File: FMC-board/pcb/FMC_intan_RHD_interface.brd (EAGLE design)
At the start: 76.5 x 69 mm, 84 parts, among them Q1 SSM3J328R, U1 4901, U2 7933, U3 ADN4663, U4 ADN4663, U5 ADN4664, U6 PDS1, U7 4901, U8 FMC_SINGLE_WIDTH_MODULE

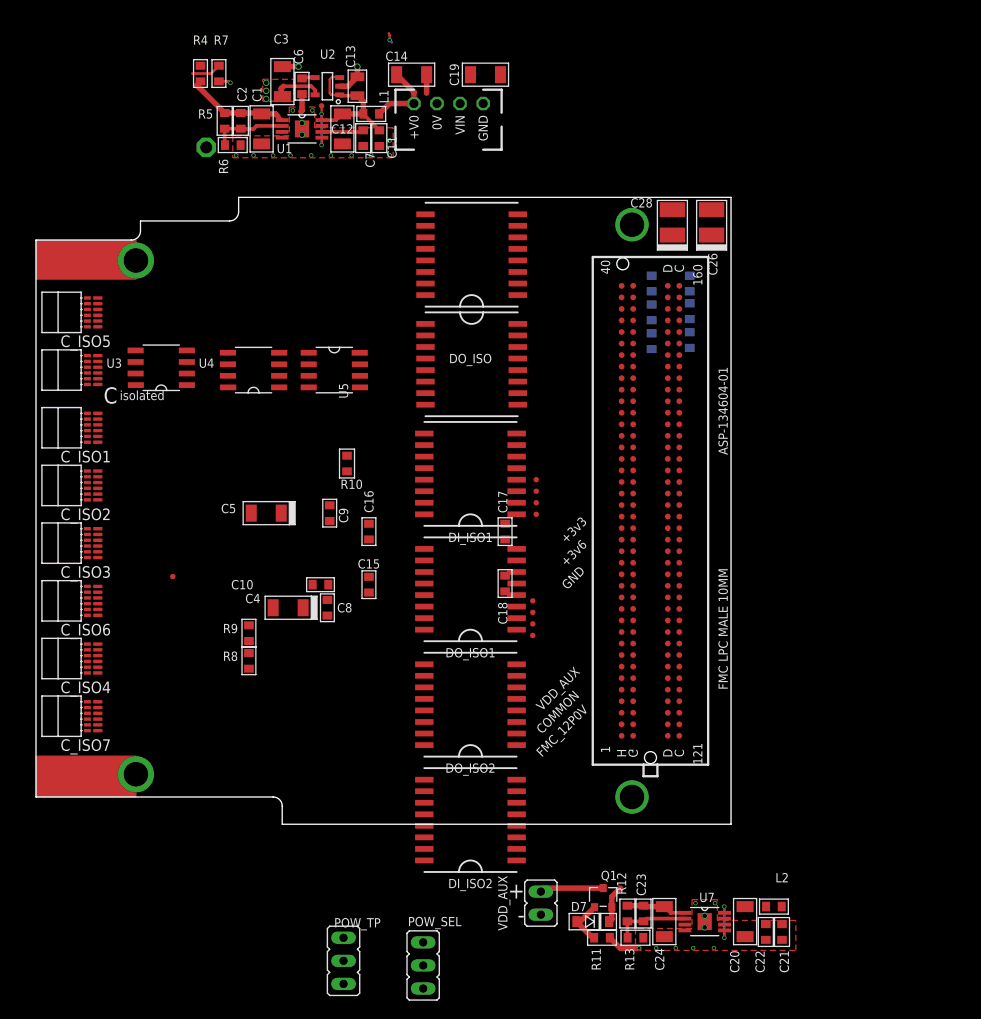
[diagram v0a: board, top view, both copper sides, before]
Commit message: added some cmos/lvds bridge components to check spacing
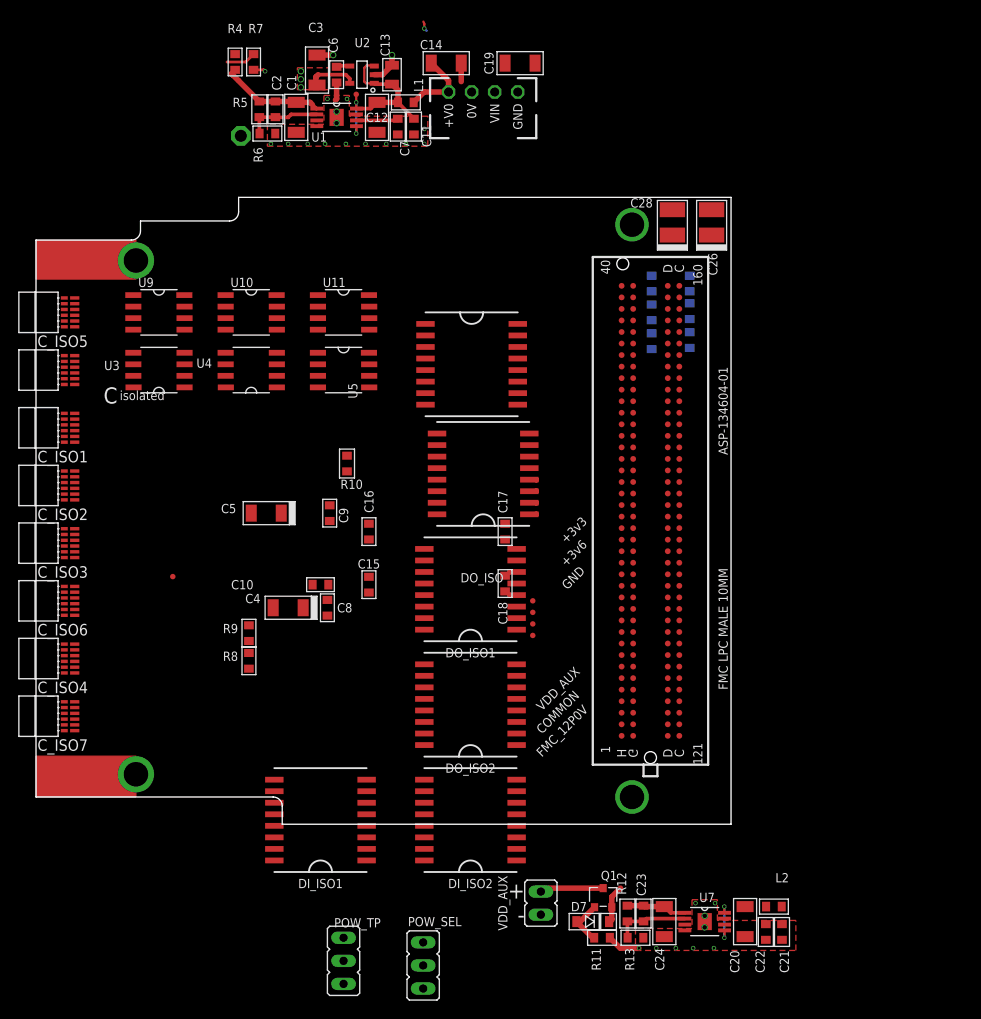
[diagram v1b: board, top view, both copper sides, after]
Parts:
- added U10, U11: ADN4663, jonnew:SOIC127P500X400-8N
- added U9: ADN4664, jonnew:SOIC127P500X400-8N
- moved DI_ISO1 41.5 mm to (-34.3, -2.54)
- moved DO_ISO 24.2 mm to (-16.4, 35.6)
- moved C14 4.02 mm to (-20.4, 80.8)
- moved C3 4.02 mm to (-34.7, 80.0)
- moved C7 4.02 mm to (-25.8, 73.8)
- moved R6 4.02 mm to (-40.1, 73.0)
- moved C19 4.02 mm to (-12.3, 80.8)
- moved C11 4.02 mm to (-24.0, 73.8)
- moved C1 4.02 mm to (-37.0, 74.8)
- moved C6 4.02 mm to (-32.5, 79.5)
- moved L1 4.02 mm to (-24.9, 76.5)
- moved R5 4.02 mm to (-41.0, 75.7)
- moved R7 4.02 mm to (-41.7, 80.9)
- moved TP1 4.02 mm to (-43.1, 72.8)
- moved U1 4.02 mm to (-32.5, 74.8)
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
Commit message: basic layout concept for 8 SPI interfaces on one FMC carrier
using existing parts, but utilizing both sides of the PCB
only added 4 ports for now to evaluate the basic stragety
there are a lot of traces that need to be split etc.
will have to switch to flatter DC-DC for this
also check if we can use 2 power supplies for 8 posrts or if we need to bump up the current capacity.
might be able to expand the back of the pcb outline behind the FMC a bit and stay within the vita spec?
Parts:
- removed C_ISO, C_ISO5, C_ISO6, C_ISO7: RHD2000-CABLE-DAQ-SIDE, RHD2000_eval_board:OMNETICS_PZN-12-AA
- removed DI_ISO, DO_ISO: ISO7640, jonnew:SOIC_WIDE_16
- removed TP1: GND-ISO, jonnew:P1-13
- removed TP_CS: CS, jonnew:TP06R
- removed TP_H1: H23, jonnew:TP06R
- removed TP_H2: H14, jonnew:TP06R
- removed TP_H3: H13, jonnew:TP06R
- removed TP_MISO1: MISO1, jonnew:TP06R
- removed TP_MISO2: MISO2, jonnew:TP06R
- removed TP_MOSI: MOSI, jonnew:TP06R
- removed TP_SCLK: SCLK, jonnew:TP06R
- added C33, C34, C35, C36, C37, C38, C39, C42, C43, C44, C47, C48, C49, C50: 100nF, RHD2000_eval_board:0603
- added C40, C41, C45, C46, C51: 10uF, jonnew:1206-POL
- added DI_ISO3, DI_ISO4: ISO7640, jonnew:SOIC_WIDE_16
- added R1, R14, R15, R2, R3: 100, RHD2000_eval_board:0603
- added U12: ADN4664, jonnew:SOIC127P500X400-8N
- added U13, U14, U15: ADN4663, jonnew:SOIC127P500X400-8N
- C17: value 100nF -> 10uF; device RHD2000_eval_board:0603 -> jonnew:1206-POL
- C4, C5: value 10uF -> 100nF; device jonnew:1206-POL -> RHD2000_eval_board:0603
- R10: value 10k -> 100; device jonnew:0603 -> RHD2000_eval_board:0603
- U11, U3: value ADN4663 -> ADN4664
- U9: value ADN4664 -> ADN4663
- moved DI_ISO1 57.3 mm to (-38.1, 54.6), flipped to the bottom, turned to 45 degrees
- moved POW_TP 56.0 mm to (24.1, -11.7)
- moved TP13 54.9 mm to (-20.1, 70.0)
- moved POW_SEL 54.7 mm to (31.6, -17.3)
- moved DI_ISO2 49.6 mm to (-29.2, 45.7), turned to 315 degrees
- moved C4 39.2 mm to (-7.62, 45.7)
- moved C17 38.1 mm to (-48.3, 45.7), flipped to the bottom
- moved R8 37.8 mm to (-62.2, 47.0), flipped to the bottom, turned to 0 degrees
- moved DO_ISO1 37.7 mm to (-38.1, 54.6), turned to 135 degrees
- moved R9 33.2 mm to (-62.2, 44.5), flipped to the bottom, turned to 0 degrees
- moved R10 31.1 mm to (-62.2, 40.6), flipped to the bottom, turned to 0 degrees
- moved U11 30.6 mm to (-54.6, 33.0), flipped to the bottom, turned to 180 degrees
- moved C8 29.8 mm to (-7.62, 35.6), turned to 0 degrees
- moved DO_ISO2 26.7 mm to (-17.8, 36.8)
- moved C18 25.9 mm to (-38.1, 33.0), flipped to the bottom, turned to 270 degrees
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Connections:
- removed net CS+_ISOLATED: C_ISO.B1, U4.7
- removed net CS-_ISOLATED: C_ISO.T1, U4.8
- removed net MISO1+_ISOLATED: C_ISO.B4, R9.1, U5.2
- removed net MISO1-_ISOLATED: C_ISO.T4, R9.2, U5.1
- removed net MISO2+_ISOLATED: C_ISO.B5, R8.1, U5.3
- removed net MISO2-_ISOLATED: C_ISO.T5, R8.2, U5.4
- removed net N$5: R10.2, U4.3
- new net CS+_ISOLATED1: C_ISO1.B1, U14.7
- new net CS+_ISOLATED2: C_ISO2.B1
- new net CS+_ISOLATED3: C_ISO3.B1, U10.7
- new net CS+_ISOLATED4: C_ISO4.B1
- new net CS-_ISOLATED1: C_ISO1.T1, U14.8
- new net CS-_ISOLATED2: C_ISO2.T1
- new net CS-_ISOLATED3: C_ISO3.T1, U10.8
- new net CS-_ISOLATED4: C_ISO4.T1
- new net MISO1+_ISOLATED1: C_ISO1.B4, R2.1, U12.2
- new net MISO1+_ISOLATED2: C_ISO2.B4, R9.1, U3.2
- new net MISO1+_ISOLATED3: C_ISO3.B4, R10.1, U5.2
- new net MISO1+_ISOLATED4: C_ISO4.B4, R15.1, U11.2
- new net MISO1-_ISOLATED1: C_ISO1.T4, R2.2, U12.1
- new net MISO1-_ISOLATED2: C_ISO2.T4, R9.2, U3.1
- new net MISO1-_ISOLATED3: C_ISO3.T4, R10.2, U5.1
- new net MISO1-_ISOLATED4: C_ISO4.T4, R15.2, U11.1
- new net MISO2+_ISOLATED1: C_ISO1.B5, R1.1, U12.3
- new net MISO2+_ISOLATED2: C_ISO2.B5, R8.1, U3.3
- new net MISO2+_ISOLATED3: C_ISO3.B5, R3.1, U5.3
- new net MISO2+_ISOLATED4: C_ISO4.B5, R14.1, U11.3
- new net MISO2-_ISOLATED1: C_ISO1.T5, R1.2, U12.4
- new net MISO2-_ISOLATED2: C_ISO2.T5, R8.2, U3.4
- new net MISO2-_ISOLATED3: C_ISO3.T5, R3.2, U5.4
- new net MISO2-_ISOLATED4: C_ISO4.T5, R14.2, U11.4
- new net N$11: C_ISO1.T3, U13.8
- new net N$14: C_ISO1.B2, U13.6
- new net N$17: C_ISO1.T2, U13.5
- new net N$18: C_ISO3.T3, U9.8
- new net N$19: C_ISO3.B2, U9.6
- new net N$2: C_ISO3.B3, U9.7
- new net N$20: C_ISO3.T2, U9.5
- new net N$21: C_ISO4.B3, U15.7
- new net N$22: C_ISO4.T3, U15.8
- new net N$23: C_ISO4.B2, U15.6
- new net N$24: C_ISO4.T2, U15.5
- new net N$9: C_ISO1.B3, U13.7
- net +3V3: now also C33.2, C37.2, C4.2, C42.2, C47.2, C8.2, DI_ISO1.P10, DI_ISO1.P16, DI_ISO2.P10, DI_ISO2.P16, DI_ISO3.P10, DI_ISO3.P16, DI_ISO4.P10, DI_ISO4.P16, DO_ISO1.P1, DO_ISO2.P1; no longer C17.2, C18.2, DI_ISO.P10, DI_ISO.P16, DO_ISO.P1
- net +3V3_ISO: now also C15.1, C17.+, C18.1, C34.1, C35.1, C36.1, C38.2, C39.2, C40.+, C41.+, C43.2, C44.2, C45.+, C46.+, C48.1, C49.1, C5.1, C50.2, C51.+, DI_ISO1.P1, DI_ISO2.P1, DI_ISO3.P1, DI_ISO4.P1, DO_ISO1.P10, DO_ISO1.P16, DO_ISO2.P10, DO_ISO2.P16, U10.1, U11.8, U12.8, U13.1, U14.1, U15.1, U3.8, U9.1; no longer C15.2, C4.+, C5.+, C8.1, DI_ISO.P1, DO_ISO.P10, DO_ISO.P16, U3.1
- net +3V6_ISO: now also C_ISO1.B6, C_ISO2.B6, C_ISO3.B6, C_ISO4.B6; no longer C_ISO.B6
- net CS: now also DO_ISO1.P5, DO_ISO2.P5; no longer DO_ISO.P5, TP_CS.TP
- net CS_ISO: now also DO_ISO1.P12, DO_ISO2.P12, U10.2, U14.2; no longer DO_ISO.P12, U4.2
- net GND: now also C33.1, C37.1, C4.1, C42.1, C47.1, C8.1, DI_ISO1.P15, DI_ISO1.P9, DI_ISO2.P15, DI_ISO2.P9, DI_ISO3.P15, DI_ISO3.P9, DI_ISO4.P15, DI_ISO4.P9, DO_ISO1.P2, DO_ISO1.P8, DO_ISO2.P2, DO_ISO2.P8; no longer C17.1, C18.1, C_ISO1.T6, C_ISO2.T6, C_ISO3.T6, C_ISO4.T6, C_ISO5.T6, C_ISO6.T6, C_ISO7.T6, DI_ISO.P15, DI_ISO.P9, DO_ISO.P2, DO_ISO.P8
- net GND_ISO: now also C15.2, C17.-, C18.2, C34.2, C35.2, C36.2, C38.1, C39.1, C40.-, C41.-, C43.1, C44.1, C45.-, C46.-, C48.2, C49.2, C5.2, C50.1, C51.-, C_ISO1.T6, C_ISO2.T6, C_ISO3.T6, C_ISO4.T6, DI_ISO1.P2, DI_ISO1.P8, DI_ISO2.P2, DI_ISO2.P8, DI_ISO3.P2, DI_ISO3.P8, DI_ISO4.P2, DI_ISO4.P8, DO_ISO1.P15, DO_ISO1.P9, DO_ISO2.P15, DO_ISO2.P9, U10.4, U11.5, U12.5, U13.4, U14.4, U15.4, U3.5, U9.4; no longer C15.1, C4.-, C5.-, C8.2, C_ISO.T6, DI_ISO.P2, DI_ISO.P8, DO_ISO.P15, DO_ISO.P9, R10.1, TP1.TP, U3.4
- net H13: now also DI_ISO1.P11, DI_ISO2.P11, DI_ISO3.P11, DI_ISO4.P11; no longer DI_ISO.P11, TP_H3.TP
- net H13_ISO: now also DI_ISO1.P6, DI_ISO2.P6, DI_ISO3.P6, DI_ISO4.P6; no longer DI_ISO.P6
- net H14: now also DI_ISO1.P12, DI_ISO2.P12, DI_ISO3.P12, DI_ISO4.P12; no longer DI_ISO.P12, TP_H2.TP
- net H14_ISO: now also DI_ISO1.P5, DI_ISO2.P5, DI_ISO3.P5, DI_ISO4.P5; no longer DI_ISO.P5
- net H23: now also DO_ISO1.P6, DO_ISO2.P6; no longer DO_ISO.P6, TP_H1.TP
- net H23_ISO: now also DO_ISO1.P11, DO_ISO2.P11, U10.3, U14.3; no longer DO_ISO.P11
- net MISO1: now also DI_ISO1.P14, DI_ISO2.P14, DI_ISO3.P14, DI_ISO4.P14; no longer DI_ISO.P14, TP_MISO1.TP
- net MISO1_ISO: now also DI_ISO1.P3, DI_ISO2.P3, DI_ISO3.P3, DI_ISO4.P3, U11.7, U12.7, U3.7; no longer DI_ISO.P3
- net MISO2: now also DI_ISO1.P13, DI_ISO2.P13, DI_ISO3.P13, DI_ISO4.P13; no longer DI_ISO.P13, TP_MISO2.TP
- net MISO2_ISO: now also DI_ISO1.P4, DI_ISO2.P4, DI_ISO3.P4, DI_ISO4.P4, U11.6, U12.6, U3.6; no longer DI_ISO.P4
- net MOSI: now also DO_ISO1.P3, DO_ISO2.P3; no longer DO_ISO.P3, TP_MOSI.TP
- net MOSI_ISO: now also DO_ISO1.P14, DO_ISO2.P14, U13.2, U15.2, U4.2, U9.2; no longer DO_ISO.P14, U3.2
- net N$12: now also C_ISO2.B3, U4.7; no longer C_ISO.B3, U3.7
- net N$13: now also C_ISO2.T3, U4.8; no longer C_ISO.T3, U3.8
- net N$15: now also C_ISO2.B2, U4.6; no longer C_ISO.B2, U3.6
- net N$16: now also C_ISO2.T2, U4.5; no longer C_ISO.T2, U3.5
- net SCLK: now also DO_ISO1.P4, DO_ISO2.P4; no longer DO_ISO.P4, TP_SCLK.TP
- net SCLK_ISO: now also DO_ISO1.P13, DO_ISO2.P13, U13.3, U15.3, U4.3, U9.3; no longer DO_ISO.P13, U3.3
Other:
- board text removed: "from FMC H23"
- board text removed: "to FMC H13"
- board text removed: "to FMC H14"
